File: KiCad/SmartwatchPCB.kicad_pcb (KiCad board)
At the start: 2 copper layers, 28.4 x 40 mm, 38 parts, among them IC1 SAML22G, IC2 TFBS4711, J1 USB_B_Micro, J2 Conn_01x04_Male, J3 Conn_01x04_Male, U1 LCD

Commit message: close to ordering first version
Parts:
- added C5: 100nF, Capacitor_SMD:C_0603_1608Metric, F.Cu at (45.3, 36.7)
- added C6: 100nF, Capacitor_SMD:C_0603_1608Metric, F.Cu at (38.4, 48.3)
- added C7: 100nF, Capacitor_SMD:C_0603_1608Metric, F.Cu at (40.6, 51.3)
- added D2: LED, LED_SMD:LED_0603_1608Metric_Castellated, F.Cu at (44.2, 40.9)
- added R4: R, Resistor_SMD:R_0603_1608Metric, F.Cu at (41.4, 43.9)
- added R5: R, Resistor_SMD:R_0603_1608Metric, F.Cu at (45.3, 38.5)
- added TP_GND1: TestPoint, TestPoint:TestPoint_Pad_D1.5mm, F.Cu at (37.6, 43.0)
- added TP_VBAT1: TestPoint, TestPoint:TestPoint_Pad_D1.5mm, F.Cu at (37.6, 46.3)
- added U2: MCP73831-2-OT, Package_TO_SOT_SMD:SOT-23-5, F.Cu at (44.3, 44.2)
- added U3: AP2112K-2.5, Package_TO_SOT_SMD:SOT-23-5, F.Cu at (44.3, 49.4)
- U1: footprint SmartwatchPCB:display -> SmartwatchPCB:display_MOUNT
- moved C2 65.7 mm to (26.3, 42.8)
- moved R3 52.4 mm to (32.8, 53.2), turned to 180 degrees
- moved TP_VLCD1 49.2 mm to (32.9, 40.2)
- moved U1 49.2 mm to (32.9, 33.6)
- moved C1 49.2 mm to (24.3, 22.1)
- moved C4 49.2 mm to (32.3, 37.8)
- moved D1 49.2 mm to (45.4, 27.5)
- moved IC1 49.2 mm to (32.4, 31.1)
- moved IC2 49.2 mm to (20.1, 27.4)
- moved J1 49.2 mm to (43.4, 27.4)
- moved J2 49.2 mm to (21.9, 44.1)
- moved R1 49.2 mm to (43.6, 27.4)
- moved R2 49.2 mm to (22.1, 22.1)
- moved SW_0 49.2 mm to (38.3, 50.5)
- moved SW_1 49.2 mm to (38.3, 46.5)
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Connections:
- J1 pad 1: Net-(J1-Pad1) -> VBUS
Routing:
- net VCC: track 12.6 -> 120.4 mm, vias 0 -> 5
- net SWCLK: track 37.2 -> 79.9 mm, vias 3 -> 6
- net SWDIO: track 39.7 -> 80.3 mm
- net KEYPAD_1: track 32.4 -> 69.0 mm, vias 0 -> 1
- net SCL: track 0.00 -> 26.1 mm, vias 0 -> 2
- net SDA: track 0.00 -> 24.6 mm, vias 0 -> 2
- net GND: track 12.8 -> 35.1 mm, vias 0 -> 15
- net VBUS: track 0.00 -> 18.1 mm
- net KEYPAD_2: track 41.2 -> 58.3 mm, vias 4 -> 5
- net KEYPAD_3: track 43.3 -> 59.4 mm, vias 5 -> 6
- net VBAT: track 0.00 -> 15.1 mm
- net VCC_LCD: track 0.00 -> 5.92 mm
- net Net-(D2-Pad1): track 0.00 -> 5.62 mm
- net Net-(D2-Pad2): track 0.00 -> 3.08 mm
- net Net-(IC1-Pad22): track 3.76 -> 6.62 mm
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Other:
- outline, holes or cut-outs redrawn
- board text added: "GND"
- board text added: "PIEZO"
- board text added: "VBAT"
- board text added: "VCC"

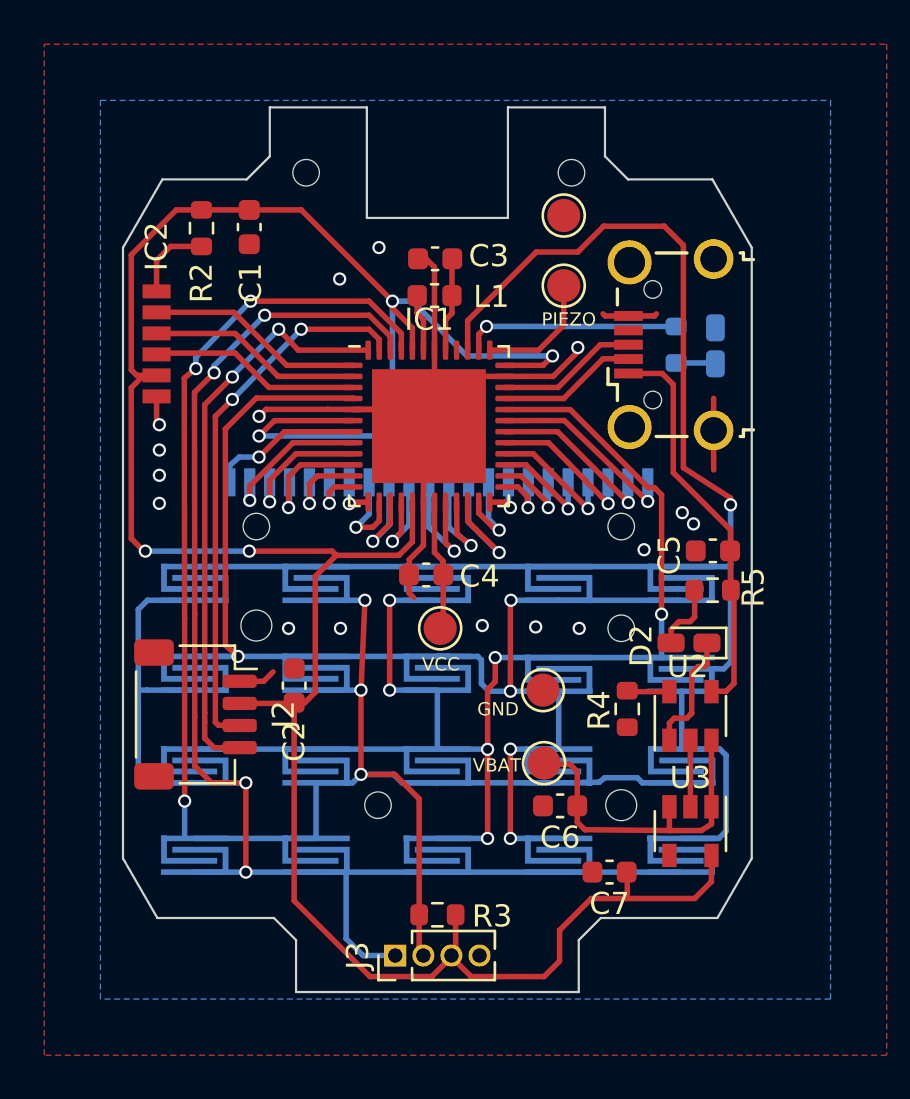
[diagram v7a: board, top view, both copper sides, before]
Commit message: swapped IR MODE to BAT ANALOG IN
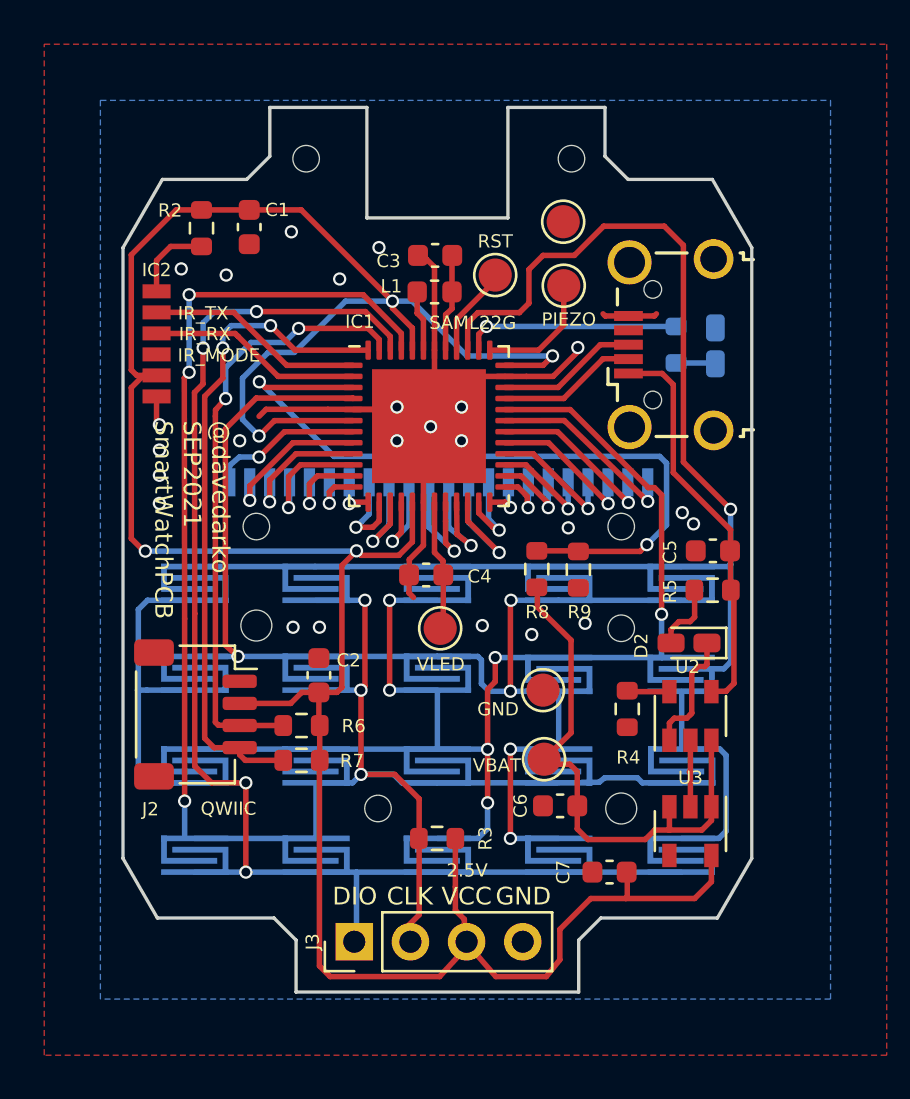
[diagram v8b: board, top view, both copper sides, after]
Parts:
- added R6: R, Resistor_SMD:R_0603_1608Metric, F.Cu at (26.7, 44.6)
- added R7: R, Resistor_SMD:R_0603_1608Metric, F.Cu at (26.7, 46.2)
- added R8: R, Resistor_SMD:R_0603_1608Metric, F.Cu at (37.3, 37.6)
- added R9: R, Resistor_SMD:R_0603_1608Metric, F.Cu at (39.2, 37.6)
- added TP_RST1: TestPoint, TestPoint:TestPoint_Pad_D1.5mm, F.Cu at (35.4, 24.3)
- J3: footprint Connector_PinHeader_1.27mm:PinHeader_1x04_P1.27mm_Vertical -> Connector_PinHeader_2.54mm:PinHeader_1x04_P2.54mm_Vertical
- moved R3 3.45 mm to (32.8, 49.7)
- moved J3 1.96 mm to (29.1, 54.4)
- moved C2 1.21 mm to (27.5, 42.4)
- moved TP_PIEZO_GND1 0.28 mm to (38.5, 21.8)
- moved TP_VBAT1 0.18 mm to (37.6, 46.2)
- moved L1 0.17 mm to (32.7, 25.0)
- moved C3 0.15 mm to (32.7, 23.4)
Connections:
- IC1 pad 3: IR_MODE -> Net-(IC1-Pad3)
- IC2 pad 4: IR_MODE -> Net-(IC2-Pad4)
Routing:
- net Net-(IC1-Pad3): track 0.00 -> 33.3 mm, vias 0 -> 2
- net IR_MODE: track 9.53 -> 0.00 mm
- net VBAT: track 15.1 -> 24.5 mm
- net VCC: track 120.4 -> 125.7 mm
- net GND: track 35.1 -> 30.2 mm, vias 15 -> 24
- net SCL: track 26.1 -> 30.0 mm
- net Net-(IC1-Pad40): track 0.00 -> 3.69 mm
- net SDA: track 24.6 -> 27.6 mm
- net SWCLK: track 79.9 -> 81.9 mm
- net KEYPAD_1: track 69.0 -> 69.6 mm
- net VCC_CORE: track 3.88 -> 4.41 mm
- net (no net): track 0.06 -> 0.00 mm, vias 1 -> 0
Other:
- board text added: "2.5V"
- board text added: "@davedarko SEP2021 SmartWatchPCB"
- board text added: "CLK"
- board text added: "DIO"
- board text added: "IR_MODE"
- board text added: "IR_RX"
- board text added: "IR_TX"
- board text added: "QWIIC"
- board text added: "RST"
- board text added: "SAML22G"
- board text added: "VLED"
